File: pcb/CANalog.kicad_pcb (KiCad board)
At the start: 2 copper layers, 80 x 45 mm, 82 parts, among them J1 PWR, J4 STM_PROG, J5 ESP_PROG, J6 AOUT, J7 CAN, Q1 DMP3099L-7, SW1 RESET, SW2 ESP_PROG, U1 BL9342, U2 MIC5504-3.3YM5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

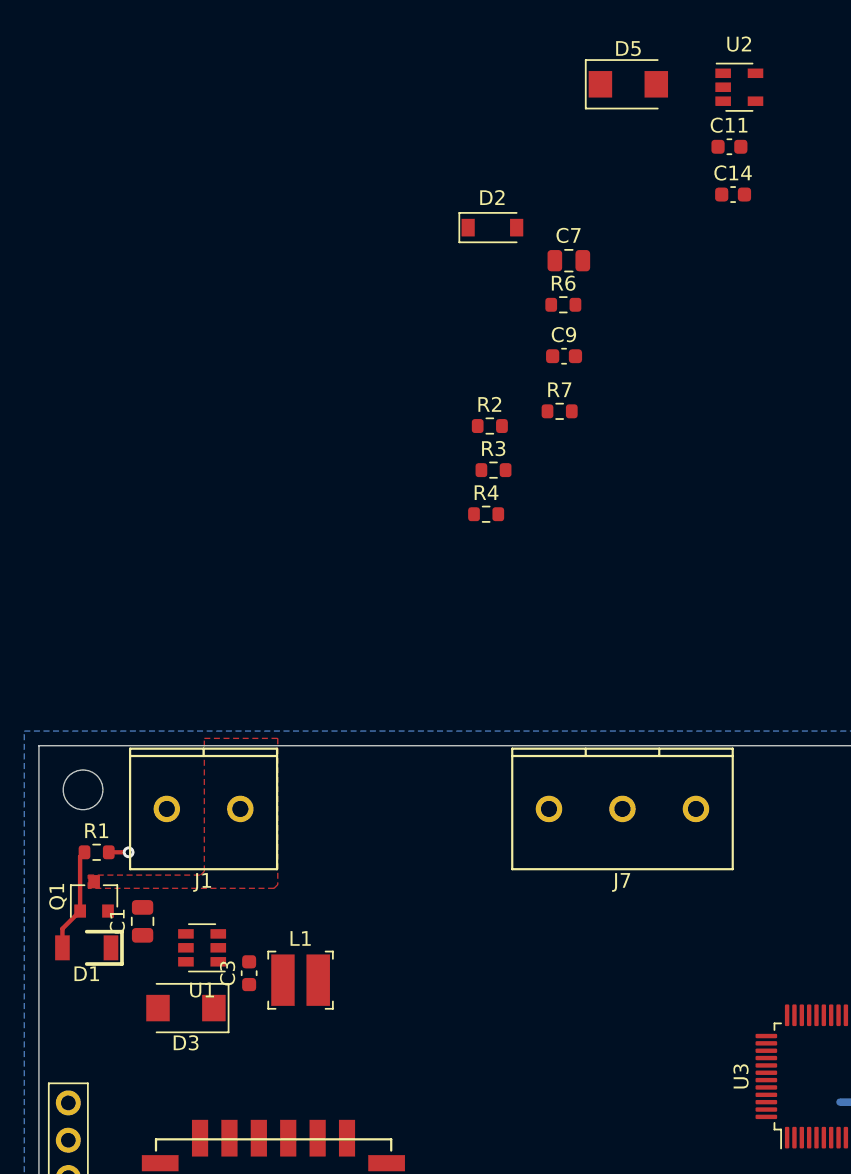
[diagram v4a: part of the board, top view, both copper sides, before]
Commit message: power supply layout
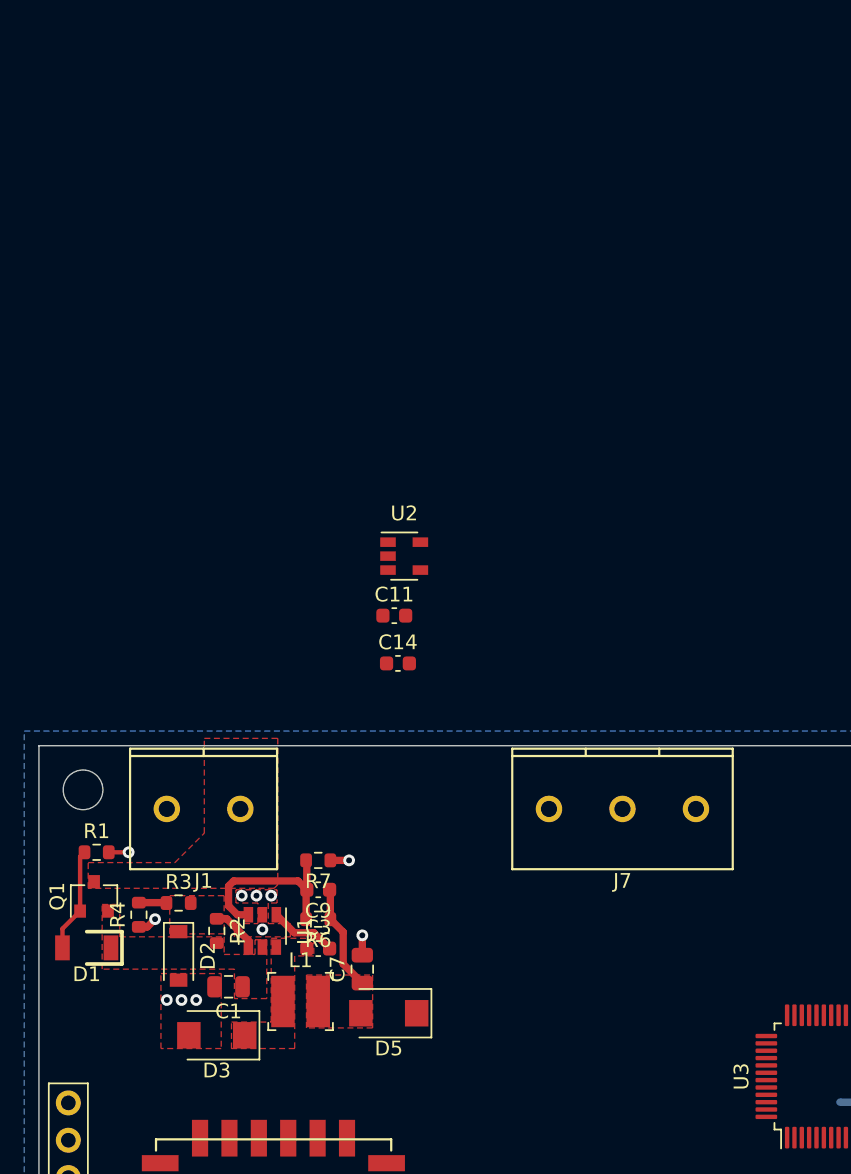
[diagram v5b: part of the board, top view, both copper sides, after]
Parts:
- moved D5 65.3 mm to (48.8, 158.2), turned to 180 degrees
- moved D2 54.0 mm to (34.5, 154.3), turned to 270 degrees
- moved C7 50.2 mm to (47.0, 155.2), turned to 90 degrees
- moved R6 45.0 mm to (44.0, 151.8), turned to 180 degrees
- moved C9 40.0 mm to (44.0, 149.8), turned to 180 degrees
- moved C11 39.2 mm to (49.2, 131.2)
- moved C14 39.2 mm to (49.4, 134.4)
- moved U2 39.2 mm to (49.9, 127.1)
- moved R2 39.1 mm to (37.1, 152.6), turned to 270 degrees
- moved R3 36.4 mm to (34.5, 150.7)
- moved R4 36.1 mm to (31.8, 151.5), turned to 90 degrees
- moved R7 34.7 mm to (44.0, 147.8), turned to 180 degrees
- moved C1 7.35 mm to (37.9, 156.4), turned to 180 degrees
- moved C3 4.99 mm to (44.0, 153.8), turned to 0 degrees
- moved U1 4.26 mm to (40.2, 152.6), turned to 270 degrees
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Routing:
- net Net-(C9-Pad2): track 0.00 -> 12.7 mm
- net /5V5: track 0.00 -> 7.27 mm
- net Net-(C3-Pad2): track 0.00 -> 4.58 mm
- net GND: track 1.35 -> 5.29 mm, vias 1 -> 11
- net Net-(D2-Pad1): track 0.00 -> 3.21 mm
- net Net-(R3-Pad1): track 0.00 -> 1.89 mm
- added copper zone on F.Cu, net /5V5
- added copper zone on F.Cu, net /Vin
- added copper zone on F.Cu, net GND
- added copper zone on F.Cu, net Net-(C3-Pad1)
- added copper zone on F.Cu, net Net-(D2-Pad1)

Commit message: Update CANalog.kicad_pcb
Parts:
- moved D5 10.1 mm to (51.0, 148.3)
- moved C7 10.1 mm to (49.1, 145.3)
- moved L1 7.02 mm to (48.1, 152.8), turned to 90 degrees
- moved D3 4.93 mm to (41.8, 158.1), turned to 270 degrees
- moved C9 1.70 mm to (44.1, 148.1)
- moved R6 1.70 mm to (44.1, 150.1)
- moved R7 1.70 mm to (44.1, 146.1)
- moved C3 1.27 mm to (44.9, 152.8), turned to 90 degrees
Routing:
- net Net-(C9-Pad2): track 12.7 -> 5.04 mm
- net /5V5: track 7.27 -> 0.00 mm
- net Net-(C3-Pad2): track 4.58 -> 3.94 mm
- net GND: track 5.29 -> 5.74 mm, vias 11 -> 10
- added copper zone on F.Cu, net Net-(C9-Pad2)

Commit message: Update CANalog.kicad_pcb
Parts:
- moved R17 61.1 mm to (62.0, 160.6)
- moved R9 57.6 mm to (58.6, 159.4), turned to 180 degrees
- moved C13 52.7 mm to (58.6, 162.4)
- moved R15 51.9 mm to (58.5, 165.4), turned to 180 degrees
- moved C5 50.7 mm to (61.1, 167.8)
- moved R5 50.4 mm to (66.4, 170.9), turned to 180 degrees
- moved D4 47.8 mm to (61.3, 171.1)
- moved U2 26.2 mm to (54.6, 152.9)
- moved C11 21.2 mm to (51.4, 152.2), turned to 270 degrees
- moved C14 20.0 mm to (57.8, 152.6), turned to 270 degrees
- moved D6 18.5 mm to (18.9, 185.1), turned to 270 degrees
- moved SW2 16.0 mm to (31.4, 163.6), turned to 270 degrees
- moved SW1 15.4 mm to (31.4, 173.9), turned to 270 degrees
- moved U4 8.19 mm to (54.5, 177.6)
- moved D3 1.92 mm to (43.5, 157.2), turned to 180 degrees
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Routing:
- net +5V: track 0.00 -> 5.67 mm, vias 0 -> 2
- net GND: vias 10 -> 16
- added copper zone on F.Cu, net +3V3
- added copper zone on F.Cu, net +5V

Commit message: Update CANalog.kicad_pcb
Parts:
- moved C10 64.2 mm to (144.5, 165.9)
- moved C2 64.2 mm to (144.0, 162.4)
- moved C4 64.2 mm to (144.5, 168.9)
- moved C6 64.2 mm to (144.0, 158.9)
- moved C8 64.2 mm to (143.8, 155.9)
- moved JP1 64.2 mm to (144.1, 173.9)
- moved FB1 64.2 mm to (144.3, 178.2)
- moved R17 62.9 mm to (0.05, 171.8)
- moved R5 62.9 mm to (4.50, 182.1)
- moved C13 62.9 mm to (-3.25, 173.6)
- moved C5 62.9 mm to (-0.80, 179.0)
- moved D4 62.9 mm to (-0.60, 182.3)
- moved R15 62.9 mm to (-3.40, 176.6)
- moved R9 62.9 mm to (-3.30, 170.6)
- moved SW1 49.2 mm to (80.0, 181.6), turned to 0 degrees
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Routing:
- net Net-(D1-Pad2): track 7.12 -> 3.00 mm
- net GND: track 5.74 -> 5.61 mm, vias 16 -> 11
- added copper zone on F.Cu, net Net-(D1-Pad2)
